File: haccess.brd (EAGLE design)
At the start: 74 x 28 mm, 22 parts

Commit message: Think I'm done?
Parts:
- added D1: (no value), SparkFun-LED:LED-0603
- added EEPROM:C1, EXPANSION_FFC:C1, HEADPHONE:C1, HEADPHONE:C3, USB_A:C1: 0.1uF, rcl:C0603
- added EEPROM:EEPROM: 24LC256, SparkFun-IC-Memory:SO08
- added EXPANSION_FFC:R1, EXPANSION_FFC:R2, USB_A:R1, USB_A:R2: 10k, rcl:R0603
- added EXPANSION_FFC:U$1: PINEBOOK-PRO-EXPANSION-CONNECTOR, pinebook_parts:FPC-C528044
- added EXPANSION_FFC:U$2, USB_A:U$1: CURRENT-LIMITINGSY6280, pinebook_parts:SOT23-5
- added HEADPHONE:C2: 1uF, rcl:C0603
- added HEADPHONE:ESD1, HEADPHONE:ESD2, HEADPHONE:ESD3, HEADPHONE:ESD4, MICROSD:ESD1, MICROSD:ESD2, MICROSD:ESD3, MICROSD:ESD4, MICROSD:ESD5, MICROSD:ESD6, MICROSD:ESD7: DIODE_ESDUAD03C05L01, pinebook_parts:DFN1608
- added HEADPHONE:HEADPHONES: C128994, pinebook_parts:AUDIO_JACK_C128994
- added HEADPHONE:R1: 12.2k, rcl:R0603
- added MPU:PROGRAM: AVR_PROGRAMMER, gone:TC2030-IDC-NL
- added R1: 160, rcl:R0603
- added SAO: FEMALE 2x3, SparkFun-Connectors:2X3
- HALL_EFFECT:U$1: value TH9245 -> HALL_EFFECT_SENSORTH9245
- moved MPU:C6 1.63 mm to (63.5, 9.14), turned to 0 degrees
- moved REG_3.3V:C8 1.30 mm to (7.37, 23.6)
- moved REG_3.3V:U$3 1.30 mm to (7.37, 21.1)
- moved HALL_EFFECT:C1 1.27 mm to (25.1, 15.5), turned to 270 degrees
- moved HALL_EFFECT:R1 1.27 mm to (27.2, 15.5), turned to 90 degrees
- moved MICROSD:C1 1.08 mm to (52.6, 2.79), turned to 0 degrees
- moved REG_3.3V:C1 0.80 mm to (7.37, 18.0)
- moved MPU:C4 0.51 mm to (50.5, 21.3)
- flipped USB_A:USB to the bottom
- renumbered U$2 to USB_A:USB
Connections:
- removed net MPU:MISO: MPU:U2.11
- removed net MPU:MOSI: MPU:U2.10
- removed net MPU:SCK: MPU:U2.9
- new net EXPANSION_FFC:ISET: EXPANSION_FFC:R1.1, EXPANSION_FFC:U$2.3
- new net EXPANSION_FFC:VOUT: EXPANSION_FFC:C1.1, EXPANSION_FFC:U$1.P$15, EXPANSION_FFC:U$1.P$16, EXPANSION_FFC:U$2.1
- new net EXP_EN: EXPANSION_FFC:R2.2, EXPANSION_FFC:U$2.4, MPU:U2.36
- new net G0: EXPANSION_FFC:U$1.P$11, MPU:U2.31
- new net G1: EXPANSION_FFC:U$1.P$10, MPU:U2.30
- new net G2: EXPANSION_FFC:U$1.P$9, MPU:U2.29
- new net G3: EXPANSION_FFC:U$1.P$8, MPU:U2.28
- new net MPU:PB1/SCK: MPU:PROGRAM.3, MPU:U2.9
- new net MPU:PB2/MOSI: MPU:PROGRAM.4, MPU:U2.10
- new net MPU:PB3/MISO: MPU:PROGRAM.1, MPU:U2.11
- new net MPU:PB7: MPU:U2.12
- new net MPU:PC7: MPU:U2.32
- new net MPU:PD6: MPU:U2.26
- new net MPU:PD7: MPU:U2.27
- new net MPU:PE2: MPU:U2.33
- new net MPU:PF0: MPU:U2.41
- new net MPU:PF1: MPU:U2.40
- new net MPU:PF4: MPU:U2.39
- new net MPU:PF5: MPU:U2.38
- new net MPU:PF6: MPU:U2.37
- new net MPU_RX: MPU:U2.20
- new net MPU_TX: MPU:U2.21
- new net N$1: D1.A, R1.1
- new net SAO1: MPU:U2.22, SAO.5
- new net SAO2: MPU:U2.25, SAO.6
- new net STATUS: MPU:U2.1, R1.2
- new net USB_A:ISET: USB_A:R1.1, USB_A:U$1.3
- new net USB_A:VOUT: USB_A:C1.1, USB_A:U$1.1, USB_A:USB.VCC
- new net USB_EN: MPU:U2.8, USB_A:R2.2, USB_A:U$1.4
- net /RST: now also MPU:PROGRAM.5
- net 3.3V: now also EEPROM:C1.1, EEPROM:EEPROM.8, EXPANSION_FFC:U$1.P$14, SAO.1
- net 3V0_CODEC: now also HEADPHONE:C2.1, HEADPHONE:C3.1, HEADPHONE:R1.2
- net 5V: now also EXPANSION_FFC:R2.1, EXPANSION_FFC:U$2.5, MPU:PROGRAM.2, USB_A:R2.1, USB_A:U$1.5; no longer USB_A:USB.VCC
- net DM2: now also EXPANSION_FFC:U$1.P$2
- net DM3: now also EXPANSION_FFC:U$1.P$5
- net DP2: now also EXPANSION_FFC:U$1.P$3
- net DP3: now also EXPANSION_FFC:U$1.P$6
- net GND: now also D1.C, EEPROM:C1.2, EEPROM:EEPROM.1, EEPROM:EEPROM.2, EEPROM:EEPROM.3, EEPROM:EEPROM.4, EEPROM:EEPROM.7, EXPANSION_FFC:C1.2, EXPANSION_FFC:R1.2, EXPANSION_FFC:U$1.P$1, EXPANSION_FFC:U$1.P$4, EXPANSION_FFC:U$1.P$7, EXPANSION_FFC:U$1.SHIELD1, EXPANSION_FFC:U$1.SHIELD2, EXPANSION_FFC:U$2.2, HEADPHONE:C1.2, HEADPHONE:C2.2, HEADPHONE:C3.2, HEADPHONE:ESD1.P$1, HEADPHONE:ESD2.P$1, HEADPHONE:ESD3.P$1, HEADPHONE:ESD4.P$1, MICROSD:ESD1.P$1, MICROSD:ESD2.P$1, MICROSD:ESD3.P$1, MICROSD:ESD4.P$1, MICROSD:ESD5.P$1, MICROSD:ESD6.P$1, MICROSD:ESD7.P$1, MPU:PROGRAM.6, SAO.2, USB_A:C1.2, USB_A:R1.2, USB_A:U$1.2
- net HPO_L: now also HEADPHONE:ESD2.P$2, HEADPHONE:HEADPHONES.B2, HEADPHONE:HEADPHONES.T2
- net HPO_R: now also HEADPHONE:ESD3.P$2, HEADPHONE:HEADPHONES.B6, HEADPHONE:HEADPHONES.T6
- net HP_DET_H: now also HEADPHONE:C1.1, HEADPHONE:ESD1.P$2, HEADPHONE:HEADPHONES.B3, HEADPHONE:HEADPHONES.T3
- net HP_GND: now also HEADPHONE:HEADPHONES.B4, HEADPHONE:HEADPHONES.T4
- net MIC_IN2P: now also HEADPHONE:ESD4.P$2, HEADPHONE:HEADPHONES.B1, HEADPHONE:HEADPHONES.T1, HEADPHONE:R1.1
- net SCL: now also EEPROM:EEPROM.6, EXPANSION_FFC:U$1.P$12, SAO.4
- net SDA: now also EEPROM:EEPROM.5, EXPANSION_FFC:U$1.P$13, SAO.3
- net SD_CLK: now also MICROSD:ESD4.P$2
- net SD_CMD: now also MICROSD:ESD5.P$2
- net SD_D0: now also MICROSD:ESD3.P$2
- net SD_D1: now also MICROSD:ESD2.P$2
- net SD_D2: now also MICROSD:ESD7.P$2
- net SD_D3: now also MICROSD:ESD6.P$2
- net SD_DET_L: now also MICROSD:ESD1.P$2
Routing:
- net DP3: track 0.00 -> 67.1 mm, vias 0 -> 2
- net DM3: track 0.00 -> 65.1 mm, vias 0 -> 2
- net USB_EN: track 0.00 -> 61.3 mm, vias 0 -> 2
- net DP2: track 0.00 -> 61.2 mm, vias 0 -> 2
- net DM2: track 0.00 -> 60.4 mm, vias 0 -> 2
- net 5V: track 84.5 -> 144.9 mm, vias 4 -> 7
- net SDA: track 2.06 -> 61.0 mm, vias 0 -> 2
- net SCL: track 2.06 -> 57.8 mm, vias 0 -> 2
- net MIC_IN2P: track 0.00 -> 26.6 mm, vias 0 -> 1
- net HPO_L: track 0.00 -> 23.3 mm, vias 0 -> 2
- net HP_GND: track 0.00 -> 22.8 mm, vias 0 -> 1
- net HP_DET_H: track 0.00 -> 22.1 mm, vias 0 -> 2
- net HPO_R: track 0.00 -> 21.9 mm, vias 0 -> 1
- net 3.3V: track 143.0 -> 161.4 mm, vias 4 -> 5
- net 3V0_CODEC: track 25.3 -> 39.9 mm
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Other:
- outline, holes or cut-outs redrawn

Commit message: I think I'm done?
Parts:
- added GPS:C1: 0.1uF, rcl:C0603
- added GPS:J1: U.FL, SparkFun-Connectors:U.FL
- added GPS:U$1: GPS-ATGM336H, pinebook_parts:ATGM336H
- moved MPU:RN2 0.57 mm to (56.9, 5.84)
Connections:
- removed net MPU:PC7: MPU:U2.32
- removed net MPU:PE2: MPU:U2.33
- new net GPS:RF_IN: GPS:J1.FEED, GPS:U$1.P$11
- new net GPS_ENABLE: GPS:U$1.P$5, MPU:U2.33
- new net PULSE: GPS:U$1.P$4, MPU:U2.32
- net /RST: now also GPS:U$1.P$9
- net 3.3V: now also GPS:C1.1, GPS:U$1.P$14, GPS:U$1.P$6, GPS:U$1.P$8
- net GND: now also GPS:C1.2, GPS:J1.1, GPS:J1.2, GPS:U$1.P$1, GPS:U$1.P$10, GPS:U$1.P$12
- net MPU_RX: now also GPS:U$1.P$2
- net MPU_TX: now also GPS:U$1.P$3
- net SCL: now also GPS:U$1.P$17
- net SDA: now also GPS:U$1.P$16
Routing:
- net /RST: track 70.9 -> 90.7 mm
- net MPU_TX: track 0.00 -> 17.2 mm, vias 0 -> 1
- net 3.3V: track 161.4 -> 176.5 mm, vias 5 -> 7
- net MPU_RX: track 0.00 -> 14.5 mm, vias 0 -> 1
- net GPS_ENABLE: track 0.00 -> 6.83 mm, vias 0 -> 1
- net SCL: track 57.8 -> 51.3 mm
- net PULSE: track 0.00 -> 4.81 mm, vias 0 -> 1
- net SDA: track 61.0 -> 56.2 mm, vias 2 -> 1
- net GPS:RF_IN: track 0.00 -> 4.24 mm
- net SD_D2: track 36.0 -> 33.1 mm
- net GND: track 42.9 -> 41.3 mm, vias 25 -> 30
- net DP2: track 61.2 -> 62.5 mm
- net DM3: track 65.1 -> 66.4 mm
- net DP3: track 67.1 -> 68.4 mm
- net DM2: track 60.4 -> 61.7 mm
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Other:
- outline, holes or cut-outs redrawn

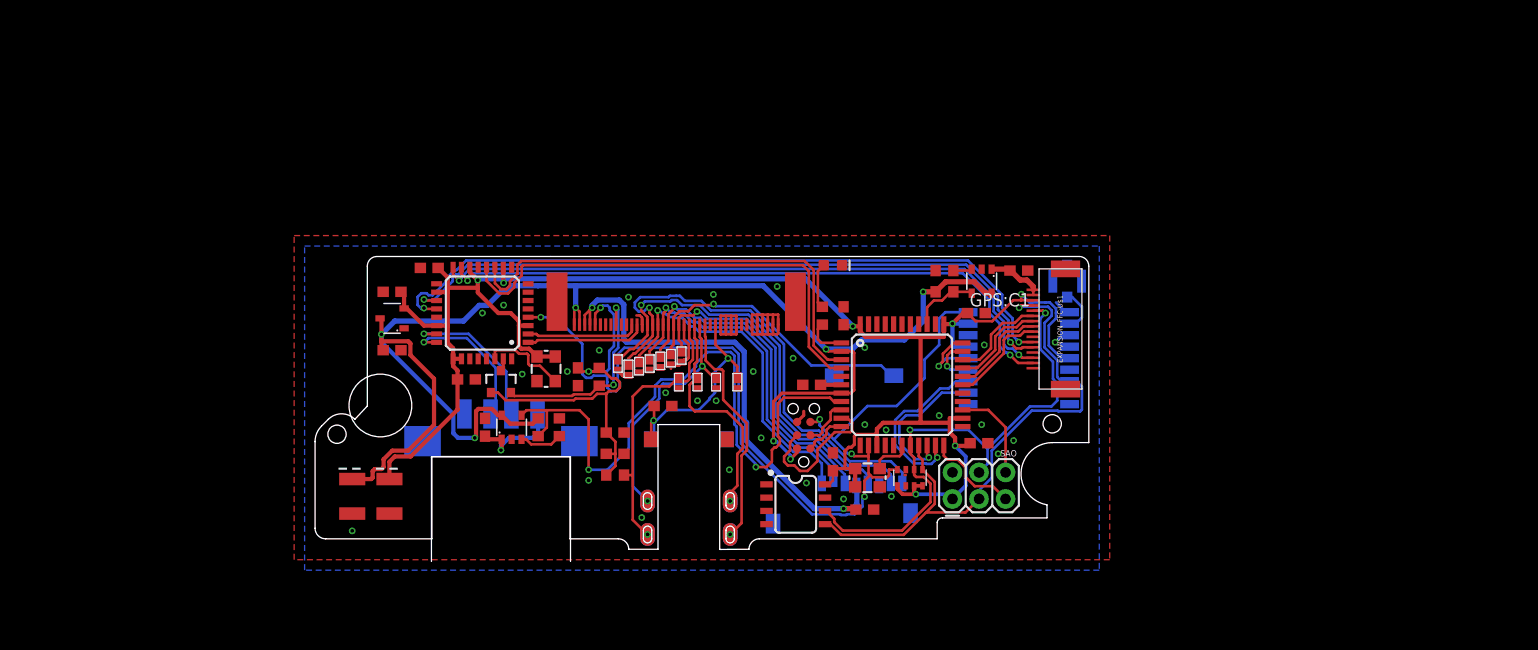
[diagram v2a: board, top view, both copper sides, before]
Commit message: More revisioning.. Now has always-available power.. but its not completed. Daughterboard dimensions completed.
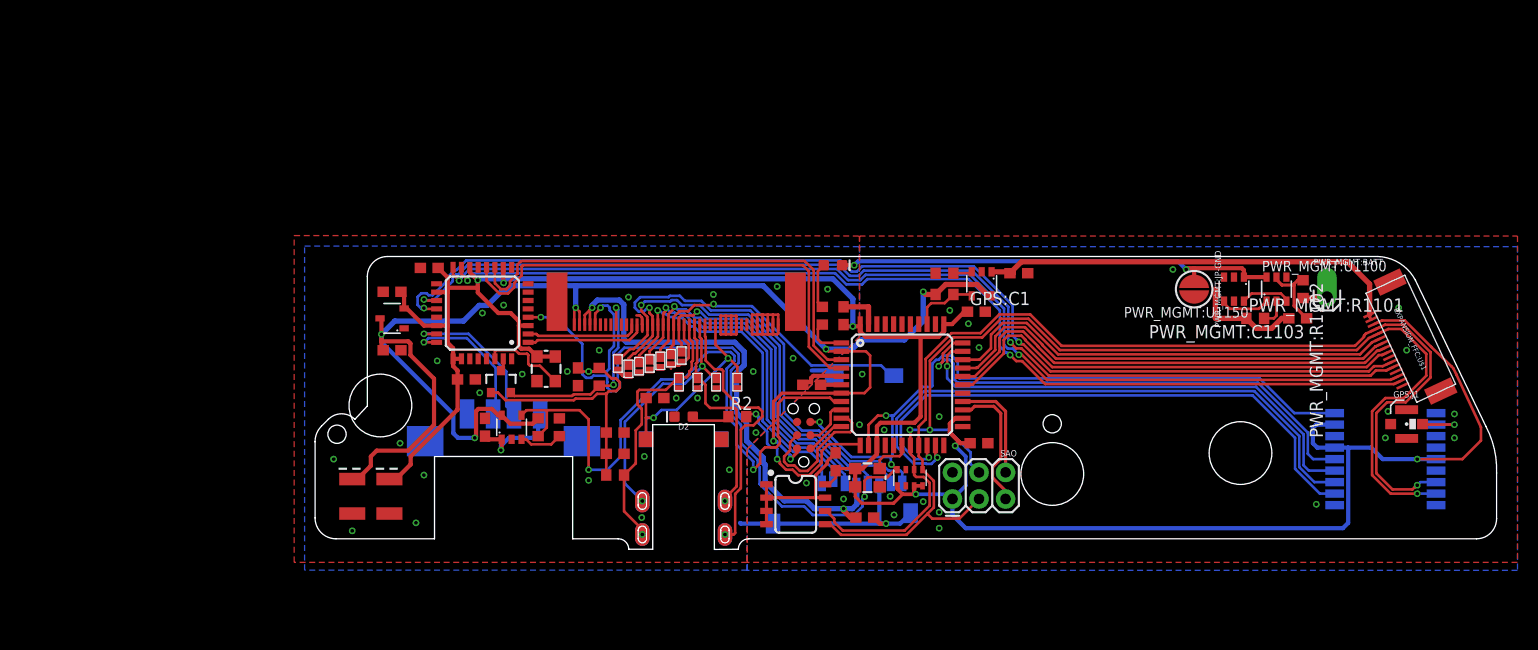
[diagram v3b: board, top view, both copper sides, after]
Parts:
- added D2: (no value), SparkFun-LED:LED-0603
- added PWR_MGMT:BATT: (no value), SparkFun-Connectors:1X01_OFFSET
- added PWR_MGMT:C1103: 0.1uF, rcl:C0603
- added PWR_MGMT:JP-GND: JUMPER-SMT_2_NO_SILK_ROUND, SparkFun-Jumpers:SMT-JUMPER_2_NO_SILK_ROUND
- added PWR_MGMT:R1101: 1k, rcl:R0603
- added PWR_MGMT:R1102: 100, rcl:R0603
- added PWR_MGMT:U1100: FS312F-G, geusebio:SOT23-6
- added PWR_MGMT:U1150: FS8205, geusebio:SOT23-6
- added R2: 160, rcl:R0603
- moved GPS:U$1 36.4 mm to (102.4, 7.62)
- moved GPS:J1 35.2 mm to (104.4, 11.0), flipped to the top, turned to 0 degrees
- moved EXPANSION_FFC:U$1 33.7 mm to (103.0, 18.3), turned to 115 degrees
- moved HEADPHONE:C1 1.08 mm to (32.5, 13.5)
- moved MICROSD:C1 0.76 mm to (52.6, 2.03)
- moved HEADPHONE:HEADPHONES 0.50 mm to (35.2, -2.29)
- moved EXPANSION_FFC:C1 0.25 mm to (67.3, 25.4)
- moved EXPANSION_FFC:R1 0.25 mm to (60.2, 25.4)
- moved EXPANSION_FFC:R2 0.25 mm to (60.2, 23.4)
- moved EXPANSION_FFC:U$2 0.25 mm to (63.8, 24.4)
- moved EEPROM:C1 0.25 mm to (49.8, 7.37)
- moved USB_A:USB 0.25 mm to (18.0, 11.9)
- moved GPS:C1 0.13 mm to (63.2, 21.7)
- renumbered REG_3.3V:C1 to PWR_MGMT:C1, REG_3.3V:C10 to PWR_MGMT:C10, REG_3.3V:C11 to PWR_MGMT:C11, REG_3.3V:C8 to PWR_MGMT:C8, REG_3.3V:U$3 to PWR_MGMT:U$3
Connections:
- removed net MPU:PB7: MPU:U2.12
- removed net MPU:PD6: MPU:U2.26
- new net AUD_STATUS: MPU:U2.12, R2.2
- new net GND_ISOLATED: EEPROM:C1.2, EEPROM:EEPROM.1, EEPROM:EEPROM.2, EEPROM:EEPROM.3, EEPROM:EEPROM.4, EEPROM:EEPROM.7, EXPANSION_FFC:C1.2, EXPANSION_FFC:R1.2, EXPANSION_FFC:U$1.P$1, EXPANSION_FFC:U$1.P$4, EXPANSION_FFC:U$1.P$7, EXPANSION_FFC:U$1.SHIELD1, EXPANSION_FFC:U$1.SHIELD2, EXPANSION_FFC:U$2.2, GPS:C1.2, GPS:J1.1, GPS:J1.2, GPS:U$1.P$1, GPS:U$1.P$10, GPS:U$1.P$12, MPU:C3.2, MPU:C4.2, MPU:C6.2, MPU:PROGRAM.6, MPU:RN2.3, MPU:RN2.6, MPU:U$2.2, MPU:U2.15, MPU:U2.23, MPU:U2.35, MPU:U2.43, MPU:U2.5, PWR_MGMT:C1103.2, PWR_MGMT:JP-GND.2, PWR_MGMT:R1101.1, PWR_MGMT:U1150.3, SAO.2
- new net MPU:PD5: MPU:U2.22
- new net N$2: D2.A, R2.1
- new net PWR_MGMT:FS_CS: PWR_MGMT:R1101.2, PWR_MGMT:U1100.2
- new net PWR_MGMT:FS_V_BATT: PWR_MGMT:C1103.1, PWR_MGMT:R1102.1, PWR_MGMT:U1100.5
- new net PWR_MGMT:OC: PWR_MGMT:U1100.3, PWR_MGMT:U1150.6
- new net PWR_MGMT:OD: PWR_MGMT:U1100.1, PWR_MGMT:U1150.4
- new net V_BATT: PWR_MGMT:BATT.1, PWR_MGMT:R1102.2
- net GND: now also D2.C, PWR_MGMT:JP-GND.1, PWR_MGMT:U1100.6, PWR_MGMT:U1150.1; no longer EEPROM:C1.2, EEPROM:EEPROM.1, EEPROM:EEPROM.2, EEPROM:EEPROM.3, EEPROM:EEPROM.4, EEPROM:EEPROM.7, EXPANSION_FFC:C1.2, EXPANSION_FFC:R1.2, EXPANSION_FFC:U$1.P$1, EXPANSION_FFC:U$1.P$4, EXPANSION_FFC:U$1.P$7, EXPANSION_FFC:U$1.SHIELD1, EXPANSION_FFC:U$1.SHIELD2, EXPANSION_FFC:U$2.2, GPS:C1.2, GPS:J1.1, GPS:J1.2, GPS:U$1.P$1, GPS:U$1.P$10, GPS:U$1.P$12, MPU:C3.2, MPU:C4.2, MPU:C6.2, MPU:PROGRAM.6, MPU:RN2.3, MPU:RN2.6, MPU:U$2.2, MPU:U2.15, MPU:U2.23, MPU:U2.35, MPU:U2.43, MPU:U2.5, SAO.2
- net SAO1: now also MPU:U2.25; no longer MPU:U2.22
- net SAO2: now also MPU:U2.26; no longer MPU:U2.25
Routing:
- net 3.3V: track 176.5 -> 241.4 mm, vias 7 -> 6
- net GND: track 41.3 -> 103.4 mm, vias 30 -> 29
- net SCL: track 51.3 -> 109.6 mm, vias 2 -> 3
- net SDA: track 56.2 -> 107.4 mm
- net PULSE: track 4.81 -> 46.3 mm
- net GPS_ENABLE: track 6.83 -> 47.8 mm
- net MPU_RX: track 14.5 -> 55.0 mm
- net MPU_TX: track 17.2 -> 57.1 mm
- net /RST: track 90.7 -> 129.7 mm, vias 4 -> 5
- net DM2: track 61.7 -> 98.1 mm
- net DP2: track 62.5 -> 98.8 mm
- net DM3: track 66.4 -> 102.6 mm
- net DP3: track 68.4 -> 104.6 mm
- net EXPANSION_FFC:VOUT: track 5.56 -> 41.7 mm
- net G3: track 9.62 -> 45.1 mm
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- added copper zone on layer 1, net GND_ISOLATED
- added copper zone on layer 16, net GND_ISOLATED
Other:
- board size 74 x 28 mm -> 113 x 28 mm
